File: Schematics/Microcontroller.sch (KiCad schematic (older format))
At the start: 23 parts, among them CON1 USB-MICRO-B, IC1 ATXMEGA256A3BU-A, J1 AVR_JTAG_Header, P1 CONN_02X08, X1 12MHz, X2 32.768KhZ

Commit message: Added power in connector in schematics. #3
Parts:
- removed C20: 1u, Capacitors_SMD:C_0603, symbol C
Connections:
- net labels removed: Vusb
- wire segments 126 -> 123
- no-connect marks 20 -> 21
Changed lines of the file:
@@
 SCL
 $Comp
-L VPP #PWR02
+L VPP #PWR15
 U 1 1 54B121F9
 P 9250 1200
-F 0 "#PWR02" H 9250 1050 60  0001 C CNN
+F 0 "#PWR15" H 9250 1050 60  0001 C CNN
 F 1 "VPP" H 9250 1350 60  0000 C CNN
 F 2 "" H 9250 1200 60  0000 C CNN
@@
 $EndComp
 $Comp
-L VPP #PWR03
+L VPP #PWR12
 U 1 1 54B1220F
 P 5800 1450
-F 0 "#PWR03" H 5800 1300 60  0001 C CNN
+F 0 "#PWR12" H 5800 1300 60  0001 C CNN
 F 1 "VPP" H 5800 1600 60  0000 C CNN
 F 2 "" H 5800 1450 60  0000 C CNN
@@
 $EndComp
 $Comp
-L GND #PWR04
+L GND #PWR13
 U 1 1 54B12386
 P 5850 5600
-F 0 "#PWR04" H 5850 5350 60  0001 C CNN
+F 0 "#PWR13" H 5850 5350 60  0001 C CNN
 F 1 "GND" H 5850 5450 60  0000 C CNN
 F 2 "" H 5850 5600 60  0000 C CNN
@@
 TMS
 $Comp
-L VPP #PWR05
+L VPP #PWR17
 U 1 1 54B12F47
 P 9350 2550
-F 0 "#PWR05" H 9350 2400 60  0001 C CNN
+F 0 "#PWR17" H 9350 2400 60  0001 C CNN
 F 1 "VPP" H 9350 2700 60  0000 C CNN
 F 2 "" H 9350 2550 60  0000 C CNN
@@
 $EndComp
 $Comp
-L GND #PWR06
+L GND #PWR18
 U 1 1 54B12FD2
 P 9350 3750
-F 0 "#PWR06" H 9350 3500 60  0001 C CNN
+F 0 "#PWR18" H 9350 3500 60  0001 C CNN
 F 1 "GND" H 9350 3600 60  0000 C CNN
 F 2 "" H 9350 3750 60  0000 C CNN
@@
 TOSC1
 $Comp
-L GND #PWR07
+L GND #PWR5
 U 1 1 54B13B7D
 P 3400 3100
-F 0 "#PWR07" H 3400 2850 60  0001 C CNN
+F 0 "#PWR5" H 3400 2850 60  0001 C CNN
 F 1 "GND" H 3400 2950 60  0000 C CNN
 F 2 "" H 3400 3100 60  0000 C CNN
@@
 $EndComp
 $Comp
-L GND #PWR08
+L GND #PWR9
 U 1 1 54B13BA4
 P 4200 3100
-F 0 "#PWR08" H 4200 2850 60  0001 C CNN
+F 0 "#PWR9" H 4200 2850 60  0001 C CNN
 F 1 "GND" H 4200 2950 60  0000 C CNN
 F 2 "" H 4200 3100 60  0000 C CNN
@@
 $EndComp
 $Comp
-L GND #PWR09
+L GND #PWR3
 U 1 1 54B13F80
 P 3150 3900
-F 0 "#PWR09" H 3150 3650 60  0001 C CNN
+F 0 "#PWR3" H 3150 3650 60  0001 C CNN
 F 1 "GND" H 3150 3750 60  0000 C CNN
 F 2 "" H 3150 3900 60  0000 C CNN
@@
 $EndComp
 $Comp
-L GND #PWR010
+L GND #PWR8
 U 1 1 54B13F86
 P 3950 3900
-F 0 "#PWR010" H 3950 3650 60  0001 C CNN
+F 0 "#PWR8" H 3950 3650 60  0001 C CNN
 F 1 "GND" H 3950 3750 60  0000 C CNN
 F 2 "" H 3950 3900 60  0000 C CNN
@@
 $EndComp
 $Comp
-L GND #PWR011
+L GND #PWR16
 U 1 1 54B15BE6
 P 9250 5850
-F 0 "#PWR011" H 9250 5600 60  0001 C CNN
+F 0 "#PWR16" H 9250 5600 60  0001 C CNN
 F 1 "GND" H 9250 5700 60  0000 C CNN
 F 2 "" H 9250 5850 60  0000 C CNN
@@
 $EndComp
 $Comp
-L GND #PWR012
+L GND #PWR20
 U 1 1 54B15BFC
 P 10450 5850
-F 0 "#PWR012" H 10450 5600 60  0001 C CNN
+F 0 "#PWR20" H 10450 5600 60  0001 C CNN
 F 1 "GND" H 10450 5700 60  0000 C CNN
 F 2 "" H 10450 5850 60  0000 C CNN
@@
 $EndComp
 $Comp
-L GND #PWR013
+L GND #PWR4
 U 1 1 54B17721
 P 3200 2200
-F 0 "#PWR013" H 3200 1950 60  0001 C CNN
+F 0 "#PWR4" H 3200 1950 60  0001 C CNN
 F 1 "GND" H 3200 2050 60  0000 C CNN
 F 2 "" H 3200 2200 60  0000 C CNN
@@
 $EndComp
 $Comp
-L VPP #PWR014
+L VPP #PWR11
 U 1 1 54B284BD
 P 4900 900
-F 0 "#PWR014" H 4900 750 60  0001 C CNN
+F 0 "#PWR11" H 4900 750 60  0001 C CNN
 F 1 "VPP" H 4900 1050 60  0000 C CNN
 F 2 "" H 4900 900 60  0000 C CNN
@@
 $EndComp
 $Comp
-L GND #PWR015
+L GND #PWR10
 U 1 1 54B28C09
 P 4250 1600
-F 0 "#PWR015" H 4250 1350 60  0001 C CNN
+F 0 "#PWR10" H 4250 1350 60  0001 C CNN
 F 1 "GND" H 4250 1450 60  0000 C CNN
 F 2 "" H 4250 1600 60  0000 C CNN
 F 3 "" H 4250 1600 60  0000 C CNN
 	1    4250 1600
-	1    0    0    -1
-$EndComp
-$Comp
-L C C20
-U 1 1 54B28ED0
-P 8700 5600
-F 0 "C20" H 8700 5700 40  0000 L CNN
-F 1 "1u" H 8706 5515 40  0000 L CNN
-F 2 "Capacitors_SMD:C_0603" H 8738 5450 30  0001 C CNN
-F 3 "" H 8700 5600 60  0000 C CNN
-	1    8700 5600
 	1    0    0    -1
 $EndComp
@@
 $EndComp
 $Comp
-L GND #PWR016
+L GND #PWR7
 U 1 1 54B26812
 P 3800 2700
-F 0 "#PWR016" H 3800 2450 60  0001 C CNN
+F 0 "#PWR7" H 3800 2450 60  0001 C CNN
 F 1 "GND" H 3800 2550 60  0000 C CNN
 F 2 "" H 3800 2700 60  0000 C CNN
@@
 $EndComp
 $Comp
-L GND #PWR017
+L GND #PWR6
 U 1 1 54B26B40
 P 3550 3600
-F 0 "#PWR017" H 3550 3350 60  0001 C CNN
+F 0 "#PWR6" H 3550 3350 60  0001 C CNN
 F 1 "GND" H 3550 3450 60  0000 C CNN
 F 2 "" H 3550 3600 60  0000 C CNN
@@
 $EndComp
 $Comp
-L GND #PWR018
+L GND #PWR21
 U 1 1 54B2A340
 P 10550 2550
-F 0 "#PWR018" H 10550 2300 60  0001 C CNN
+F 0 "#PWR21" H 10550 2300 60  0001 C CNN
 F 1 "GND" H 10550 2400 60  0000 C CNN
 F 2 "" H 10550 2550 60  0000 C CNN
@@
 $EndComp
 $Comp
-L VPP #PWR019
+L VPP #PWR19
 U 1 1 54B2B24F
 P 9850 1850
-F 0 "#PWR019" H 9850 1700 60  0001 C CNN
+F 0 "#PWR19" H 9850 1700 60  0001 C CNN
 F 1 "VPP" H 9850 2000 60  0000 C CNN
 F 2 "" H 9850 1850 60  0000 C CNN
@@
 	1    0    0    -1
 $EndComp
-Text HLabel 8550 5350 0    60   Output ~ 0
-Vusb
 $Comp
 L ATXMEGA256A3BU-A IC1
@@
 $EndComp
 $Comp
-L GND #PWR020
+L GND #PWR14
 U 1 1 54C80C62
 P 8900 4450
-F 0 "#PWR020" H 8900 4200 60  0001 C CNN
+F 0 "#PWR14" H 8900 4200 60  0001 C CNN
 F 1 "GND" H 8900 4300 60  0000 C CNN
 F 2 "" H 8900 4450 60  0000 C CNN
@@
 Connection ~ 4500 1500
 Connection ~ 4250 1500
-Wire Wire Line
-	8550 5350 9400 5350
-Wire Wire Line
-	8700 5350 8700 5400
-Wire Wire Line
-	8700 5800 9250 5800
 Connection ~ 9250 5800
 Wire Wire Line
@@
 Wire Wire Line
 	10550 2450 10500 2450
-Connection ~ 8700 5350
 Wire Bus Line
 	4250 5150 4100 5150
@@
 	7650 3450 7650 3650
 Connection ~ 7650 3650
+NoConn ~ 9400 5350
 $EndSCHEMATC

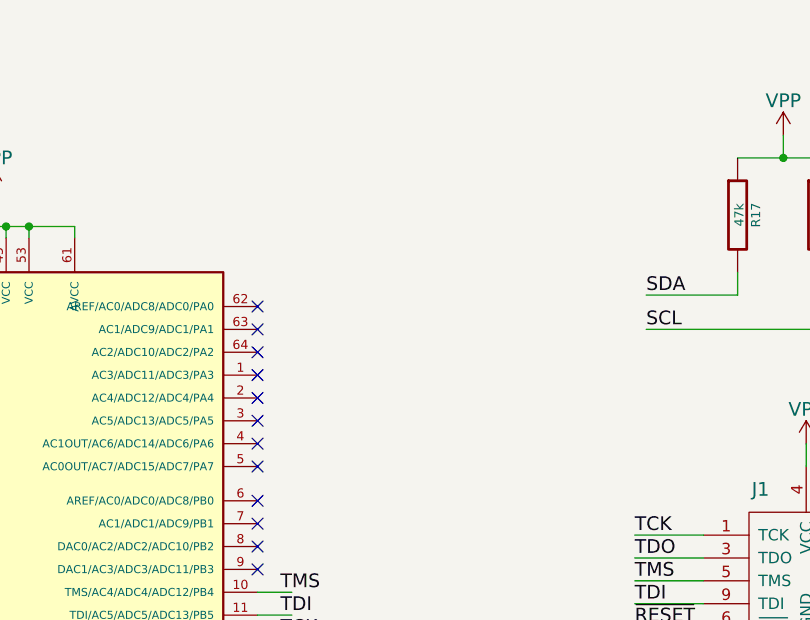
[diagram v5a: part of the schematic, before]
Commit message: Added some switches for interface #7
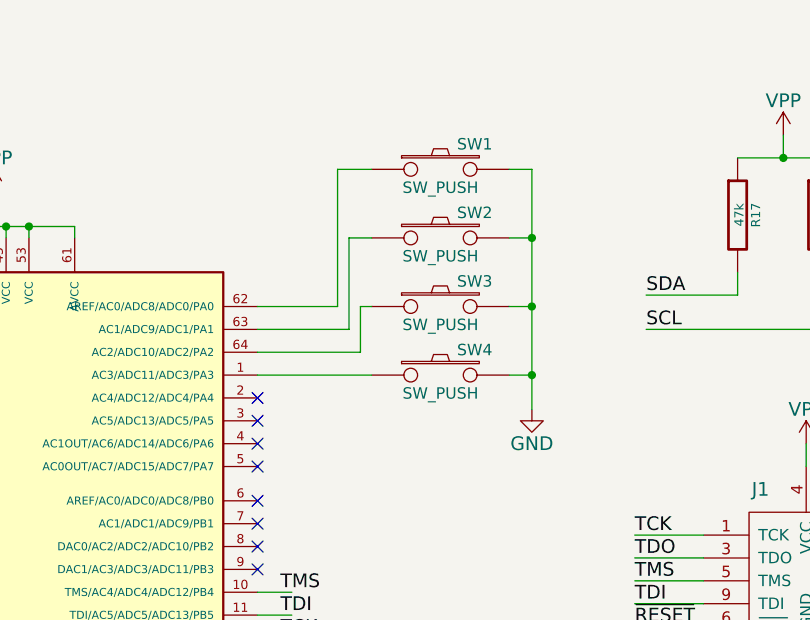
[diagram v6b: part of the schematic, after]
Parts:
- added SW1, SW2, SW3, SW4: SW_PUSH, symbol SW_PUSH
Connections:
- wire segments 123 -> 138
- no-connect marks 21 -> 17
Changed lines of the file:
@@
 SCL
 $Comp
-L VPP #PWR15
+L VPP #PWR14
 U 1 1 54B121F9
 P 9250 1200
-F 0 "#PWR15" H 9250 1050 60  0001 C CNN
+F 0 "#PWR14" H 9250 1050 60  0001 C CNN
 F 1 "VPP" H 9250 1350 60  0000 C CNN
 F 2 "" H 9250 1200 60  0000 C CNN
@@
 $EndComp
 $Comp
-L VPP #PWR12
+L VPP #PWR10
 U 1 1 54B1220F
 P 5800 1450
-F 0 "#PWR12" H 5800 1300 60  0001 C CNN
+F 0 "#PWR10" H 5800 1300 60  0001 C CNN
 F 1 "VPP" H 5800 1600 60  0000 C CNN
 F 2 "" H 5800 1450 60  0000 C CNN
@@
 $EndComp
 $Comp
-L GND #PWR13
+L GND #PWR11
 U 1 1 54B12386
 P 5850 5600
-F 0 "#PWR13" H 5850 5350 60  0001 C CNN
+F 0 "#PWR11" H 5850 5350 60  0001 C CNN
 F 1 "GND" H 5850 5450 60  0000 C CNN
 F 2 "" H 5850 5600 60  0000 C CNN
@@
 TMS
 $Comp
-L VPP #PWR17
+L VPP #PWR16
 U 1 1 54B12F47
 P 9350 2550
-F 0 "#PWR17" H 9350 2400 60  0001 C CNN
+F 0 "#PWR16" H 9350 2400 60  0001 C CNN
 F 1 "VPP" H 9350 2700 60  0000 C CNN
 F 2 "" H 9350 2550 60  0000 C CNN
@@
 $EndComp
 $Comp
-L GND #PWR18
+L GND #PWR17
 U 1 1 54B12FD2
 P 9350 3750
-F 0 "#PWR18" H 9350 3500 60  0001 C CNN
+F 0 "#PWR17" H 9350 3500 60  0001 C CNN
 F 1 "GND" H 9350 3600 60  0000 C CNN
 F 2 "" H 9350 3750 60  0000 C CNN
@@
 TOSC1
 $Comp
-L GND #PWR5
+L GND #PWR3
 U 1 1 54B13B7D
 P 3400 3100
-F 0 "#PWR5" H 3400 2850 60  0001 C CNN
+F 0 "#PWR3" H 3400 2850 60  0001 C CNN
 F 1 "GND" H 3400 2950 60  0000 C CNN
 F 2 "" H 3400 3100 60  0000 C CNN
@@
 $EndComp
 $Comp
-L GND #PWR9
+L GND #PWR7
 U 1 1 54B13BA4
 P 4200 3100
-F 0 "#PWR9" H 4200 2850 60  0001 C CNN
+F 0 "#PWR7" H 4200 2850 60  0001 C CNN
 F 1 "GND" H 4200 2950 60  0000 C CNN
 F 2 "" H 4200 3100 60  0000 C CNN
@@
 $EndComp
 $Comp
-L GND #PWR3
+L GND #PWR1
 U 1 1 54B13F80
 P 3150 3900
-F 0 "#PWR3" H 3150 3650 60  0001 C CNN
+F 0 "#PWR1" H 3150 3650 60  0001 C CNN
 F 1 "GND" H 3150 3750 60  0000 C CNN
 F 2 "" H 3150 3900 60  0000 C CNN
@@
 $EndComp
 $Comp
-L GND #PWR8
+L GND #PWR6
 U 1 1 54B13F86
 P 3950 3900
-F 0 "#PWR8" H 3950 3650 60  0001 C CNN
+F 0 "#PWR6" H 3950 3650 60  0001 C CNN
 F 1 "GND" H 3950 3750 60  0000 C CNN
 F 2 "" H 3950 3900 60  0000 C CNN
@@
 $EndComp
 $Comp
-L GND #PWR16
+L GND #PWR15
 U 1 1 54B15BE6
 P 9250 5850
-F 0 "#PWR16" H 9250 5600 60  0001 C CNN
+F 0 "#PWR15" H 9250 5600 60  0001 C CNN
 F 1 "GND" H 9250 5700 60  0000 C CNN
 F 2 "" H 9250 5850 60  0000 C CNN
@@
 $EndComp
 $Comp
-L GND #PWR20
+L GND #PWR19
 U 1 1 54B15BFC
 P 10450 5850
-F 0 "#PWR20" H 10450 5600 60  0001 C CNN
+F 0 "#PWR19" H 10450 5600 60  0001 C CNN
 F 1 "GND" H 10450 5700 60  0000 C CNN
 F 2 "" H 10450 5850 60  0000 C CNN
@@
 $EndComp
 $Comp
-L GND #PWR4
+L GND #PWR2
 U 1 1 54B17721
 P 3200 2200
-F 0 "#PWR4" H 3200 1950 60  0001 C CNN
+F 0 "#PWR2" H 3200 1950 60  0001 C CNN
 F 1 "GND" H 3200 2050 60  0000 C CNN
 F 2 "" H 3200 2200 60  0000 C CNN
@@
 $EndComp
 $Comp
-L VPP #PWR11
+L VPP #PWR9
 U 1 1 54B284BD
 P 4900 900
-F 0 "#PWR11" H 4900 750 60  0001 C CNN
+F 0 "#PWR9" H 4900 750 60  0001 C CNN
 F 1 "VPP" H 4900 1050 60  0000 C CNN
 F 2 "" H 4900 900 60  0000 C CNN
@@
 $EndComp
 $Comp
-L GND #PWR10
+L GND #PWR8
 U 1 1 54B28C09
 P 4250 1600
-F 0 "#PWR10" H 4250 1350 60  0001 C CNN
+F 0 "#PWR8" H 4250 1350 60  0001 C CNN
 F 1 "GND" H 4250 1450 60  0000 C CNN
 F 2 "" H 4250 1600 60  0000 C CNN
@@
 $EndComp
 $Comp
-L GND #PWR7
+L GND #PWR5
 U 1 1 54B26812
 P 3800 2700
-F 0 "#PWR7" H 3800 2450 60  0001 C CNN
+F 0 "#PWR5" H 3800 2450 60  0001 C CNN
 F 1 "GND" H 3800 2550 60  0000 C CNN
 F 2 "" H 3800 2700 60  0000 C CNN
@@
 $EndComp
 $Comp
-L GND #PWR6
+L GND #PWR4
 U 1 1 54B26B40
 P 3550 3600
-F 0 "#PWR6" H 3550 3350 60  0001 C CNN
+F 0 "#PWR4" H 3550 3350 60  0001 C CNN
 F 1 "GND" H 3550 3450 60  0000 C CNN
 F 2 "" H 3550 3600 60  0000 C CNN
@@
 $EndComp
 $Comp
-L GND #PWR21
+L GND #PWR20
 U 1 1 54B2A340
 P 10550 2550
-F 0 "#PWR21" H 10550 2300 60  0001 C CNN
+F 0 "#PWR20" H 10550 2300 60  0001 C CNN
 F 1 "GND" H 10550 2400 60  0000 C CNN
 F 2 "" H 10550 2550 60  0000 C CNN
@@
 $EndComp
 $Comp
-L VPP #PWR19
+L VPP #PWR18
 U 1 1 54B2B24F
 P 9850 1850
-F 0 "#PWR19" H 9850 1700 60  0001 C CNN
+F 0 "#PWR18" H 9850 1700 60  0001 C CNN
 F 1 "VPP" H 9850 2000 60  0000 C CNN
 F 2 "" H 9850 1850 60  0000 C CNN
@@
 NoConn ~ 6950 2450
 NoConn ~ 6950 2350
-NoConn ~ 6950 2250
-NoConn ~ 6950 2150
-NoConn ~ 6950 2050
-NoConn ~ 6950 1950
 $Comp
 L CONN_02X08 P1
@@
 $EndComp
 $Comp
-L GND #PWR14
+L GND #PWR13
 U 1 1 54C80C62
 P 8900 4450
-F 0 "#PWR14" H 8900 4200 60  0001 C CNN
+F 0 "#PWR13" H 8900 4200 60  0001 C CNN
 F 1 "GND" H 8900 4300 60  0000 C CNN
 F 2 "" H 8900 4450 60  0000 C CNN
 F 3 "" H 8900 4450 60  0000 C CNN
 	1    8900 4450
+	1    0    0    -1
+$EndComp
+NoConn ~ 9400 5350
+$Comp
+L SW_PUSH SW1
+U 1 1 54C97108
+P 7750 1350
+F 0 "SW1" H 7900 1460 50  0000 C CNN
+F 1 "SW_PUSH" H 7750 1270 50  0000 C CNN
+F 2 "" H 7750 1350 60  0000 C CNN
+F 3 "" H 7750 1350 60  0000 C CNN
+	1    7750 1350
+	1    0    0    -1
+$EndComp
+$Comp
+L SW_PUSH SW2
+U 1 1 54C971DE
+P 7750 1650
+F 0 "SW2" H 7900 1760 50  0000 C CNN
+F 1 "SW_PUSH" H 7750 1570 50  0000 C CNN
+F 2 "" H 7750 1650 60  0000 C CNN
+F 3 "" H 7750 1650 60  0000 C CNN
+	1    7750 1650
+	1    0    0    -1
+$EndComp
+$Comp
+L SW_PUSH SW3
+U 1 1 54C9721C
+P 7750 1950
+F 0 "SW3" H 7900 2060 50  0000 C CNN
+F 1 "SW_PUSH" H 7750 1870 50  0000 C CNN
+F 2 "" H 7750 1950 60  0000 C CNN
+F 3 "" H 7750 1950 60  0000 C CNN
+	1    7750 1950
+	1    0    0    -1
+$EndComp
+$Comp
+L SW_PUSH SW4
+U 1 1 54C97263
+P 7750 2250
+F 0 "SW4" H 7900 2360 50  0000 C CNN
+F 1 "SW_PUSH" H 7750 2170 50  0000 C CNN
+F 2 "" H 7750 2250 60  0000 C CNN
+F 3 "" H 7750 2250 60  0000 C CNN
+	1    7750 2250
 	1    0    0    -1
 $EndComp
@@
 	7650 3450 7650 3650
 Connection ~ 7650 3650
-NoConn ~ 9400 5350
+Wire Wire Line
+	6950 2250 7450 2250
+Wire Wire Line
+	7450 1950 7400 1950
+Wire Wire Line
+	7400 1950 7400 2150
+Wire Wire Line
+	7400 2150 6950 2150
+Wire Wire Line
+	6950 2050 7350 2050
+Wire Wire Line
+	7350 2050 7350 1650
+Wire Wire Line
+	7350 1650 7450 1650
+Wire Wire Line
+	7450 1350 7300 1350
+Wire Wire Line
+	7300 1350 7300 1950
+Wire Wire Line
+	7300 1950 6950 1950
+Wire Wire Line
+	8050 1350 8150 1350
+Wire Wire Line
+	8150 1350 8150 2400
+Wire Wire Line
+	8050 2250 8150 2250
+Connection ~ 8150 2250
+Wire Wire Line
+	8050 1950 8150 1950
+Connection ~ 8150 1950
+Wire Wire Line
+	8050 1650 8150 1650
+Connection ~ 8150 1650
+$Comp
+L GND #PWR12
+U 1 1 54C97F8A
+P 8150 2400
+F 0 "#PWR12" H 8150 2150 60  0001 C CNN
+F 1 "GND" H 8150 2250 60  0000 C CNN
+F 2 "" H 8150 2400 60  0000 C CNN
+F 3 "" H 8150 2400 60  0000 C CNN
+	1    8150 2400
+	1    0    0    -1
+$EndComp
 $EndSCHEMATC
